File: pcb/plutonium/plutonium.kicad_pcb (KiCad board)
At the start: 2 copper layers, 272.5 x 73.5 mm, 58 parts, among them J1 Conn_01x04, J2 Conn_01x04, K1 diode-choc, K10 diode-choc, K11 diode-choc, K12 diode-choc, K13 diode-choc, K14 diode-choc, K15 diode-choc, K16 diode-choc, K17 diode-choc, K18 diode-choc, K19 diode-choc, K2 diode-choc, K20 diode-choc, K21 diode-choc, K22 diode-choc, K23 diode-choc, K24 diode-choc, K25 diode-choc, K26 diode-choc, K27 diode-choc, K28 diode-choc, K29 diode-choc, K3 diode-choc, K30 diode-choc, K4 diode-choc, K5 diode-choc, K6 diode-choc, K7 diode-choc, K8 diode-choc, K9 diode-choc, U1 xiao-ble, U2 xiao-ble, U3 MT25QL128ABA1ESE

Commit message: [pcb] Plutonium: first revision
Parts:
- removed the REF** at (126.1, 113.2)
- J1, J2: value Conn_01x04 -> debug-port; footprint keeb-libs:debug-port-single-side -> misc:debug-port-single-side
- U1: footprint xiao:xiao-ble-smd -> xiao:xiao-ble-smd-cutout
- moved REF** 73.6 mm to (98.1, 112.7)
- moved REF** 65.6 mm to (203.6, 112.0)
- moved REF** 62.1 mm to (189.6, 112.2)
- moved REF** 48.2 mm to (84.1, 112.7)
- moved BT2 47.9 mm to (171.9, 94.2)
- moved H3 47.9 mm to (155.1, 134.7)
- moved H4 47.9 mm to (155.1, 70.2)
- moved K28 47.9 mm to (172.1, 135.2)
- moved LCD1 47.9 mm to (156.6, 102.7)
- moved R1 47.9 mm to (156.1, 87.2)
- moved REF** 47.9 mm to (173.1, 66.7)
- moved REF** 47.9 mm to (171.9, 66.7)
- moved REF** 47.9 mm to (175.1, 66.7)
- moved U2 47.9 mm to (168.1, 78.5)
- moved U3 47.9 mm to (154.9, 81.7)
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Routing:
- net C1: track 165.7 -> 167.3 mm
- net C1_L: track 173.5 -> 175.1 mm
- net C3_L: track 143.4 -> 144.0 mm
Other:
- board size 272.5 x 73.5 mm -> 278.5 x 73.5 mm

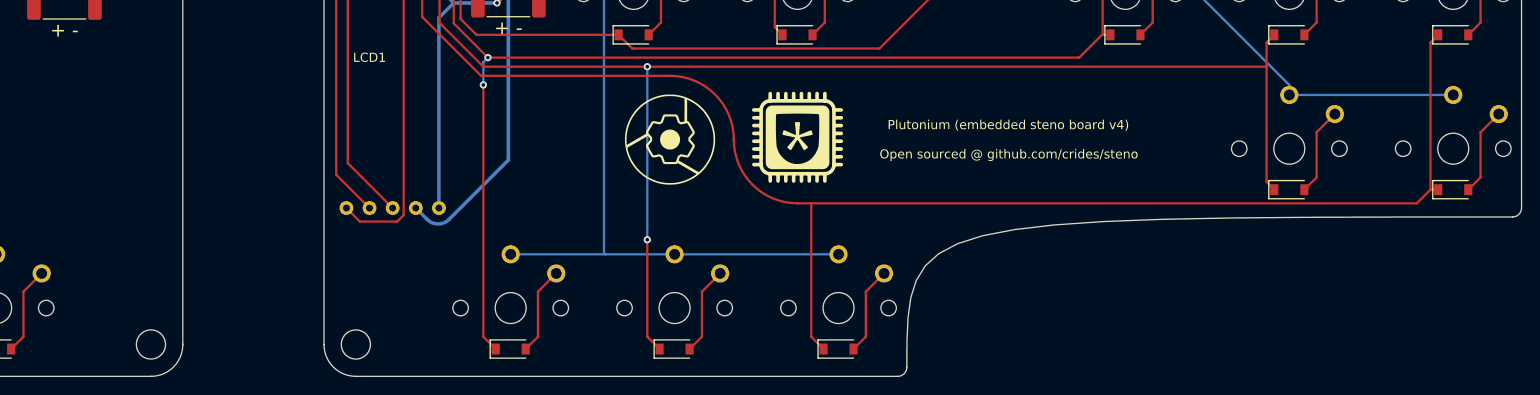
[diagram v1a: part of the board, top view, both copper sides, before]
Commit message: [pcb] Plutonium: add screen mounting and JLC tooling holes
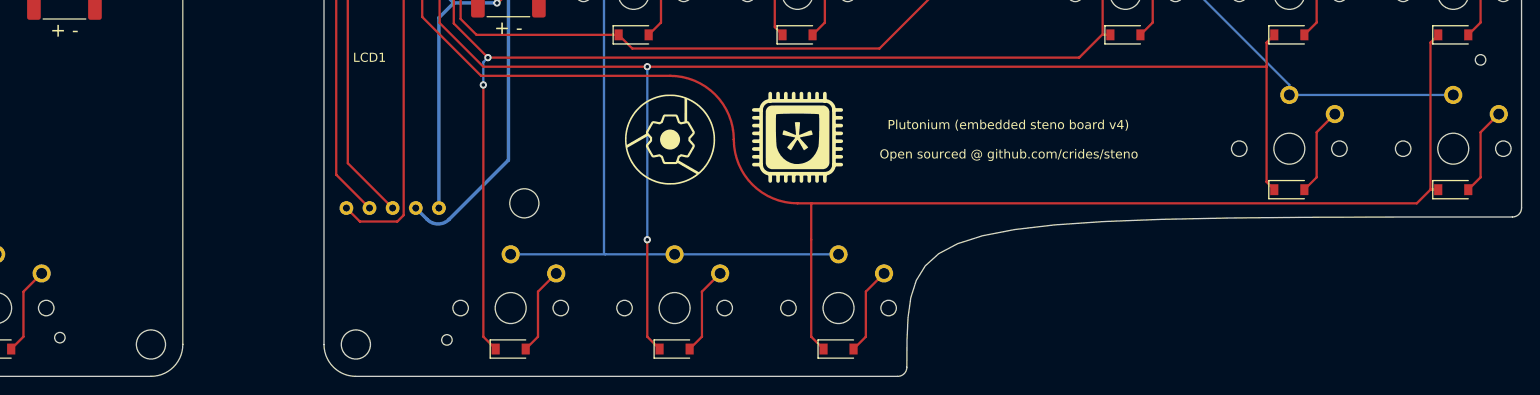
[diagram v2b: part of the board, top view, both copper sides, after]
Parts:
- added REF**: jlc-tooling-hole, misc:jlc-tooling-hole, F.Cu at (122.6, 134.0)
- added REF**: MountingHole_3.2mm_M3, MountingHole:MountingHole_3.2mm_M3, F.Cu at (173.6, 119.2)
- added REF**: jlc-tooling-hole, misc:jlc-tooling-hole, F.Cu at (165.1, 134.2)
- added REF**: jlc-tooling-hole, misc:jlc-tooling-hole, F.Cu at (278.6, 103.5)
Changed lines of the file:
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@@
+  )
+  (footprint "MountingHole:MountingHole_3.2mm_M3" (layer "F.Cu")
+    (at 173.615832 119.20203)
+    (descr "Mounting Hole 3.2mm, no annular, M3")
+    (tags "mounting hole 3.2mm no annular m3")
+    (attr board_only exclude_from_pos_files exclude_from_bom)
+    (fp_text reference "REF**" (at 0 -4.2) (layer "F.SilkS") hide
+      (effects (font (size 1 1) (thickness 0.15)))
+    )
+    (fp_text value "MountingHole_3.2mm_M3" (at 0 4.2) (layer "F.Fab")
+      (effects (font (size 1 1) (thickness 0.15)))
+    )
+    (fp_text user "${REFERENCE}" (at 0.3 0) (layer "F.Fab")
+      (effects (font (size 1 1) (thickness 0.15)))
+    )
+    (fp_circle (center 0 0) (end 3.2 0) (layer "Cmts.User") (width 0.15) (fill none))
+    (fp_circle (center 0 0) (end 3.45 0) (layer "F.CrtYd") (width 0.05) (fill none))
+    (pad "" np_thru_hole circle locked (at 0 0) (size 3.2 3.2) (drill 3.2) (layers *.Cu *.Mask))
   )
   (footprint "MountingHole:MountingHole_3.2mm_M3" (layer "F.Cu")
@@
     (pad "" np_thru_hole circle (at 0 -0.254) (size 0.7874 0.7874) (drill 0.7874) (layers *.Cu *.Mask))
   )
+  (footprint "misc:jlc-tooling-hole" (layer "F.Cu")
+    (at 165.115832 134.20203)
+    (attr through_hole board_only exclude_from_pos_files exclude_from_bom)
+    (fp_text reference "REF**" (at 0 -4 unlocked) (layer "F.SilkS") hide
+      (effects (font (size 1 1) (thickness 0.15)))
+    )
+    (fp_text value "jlc-tooling-hole" (at 0 1.5 unlocked) (layer "F.Fab")
+      (effects (font (size 1 1) (thickness 0.15)))
+    )
+    (pad "" np_thru_hole circle (at 0 0) (size 1.3 1.3) (drill 1.152) (layers *.Mask))
+  )
   (footprint "Connector_JST:JST_PH_S2B-PH-SM4-TB_1x02-1MP_P2.00mm_Horizontal" (layer "F.Cu")
     (at 171.865834 94.202021)
@@
     (pad "4" thru_hole oval (at 3.81 0 90) (size 1.2 1.2) (drill 0.7) (layers *.Cu "F.Mask")
       (net 4 "SWC") (pinfunction "SWC") (pintype "output"))
+  )
+  (footprint "misc:jlc-tooling-hole" (layer "F.Cu")
+    (at 278.615832 103.45203)
+    (attr through_hole board_only exclude_from_pos_files exclude_from_bom)
+    (fp_text reference "REF**" (at 0 -4 unlocked) (layer "F.SilkS") hide
+      (effects (font (size 1 1) (thickness 0.15)))
+    )
+    (fp_text value "jlc-tooling-hole" (at 0 1.5 unlocked) (layer "F.Fab")
+      (effects (font (size 1 1) (thickness 0.15)))
+    )
+    (pad "" np_thru_hole circle (at 0 0) (size 1.3 1.3) (drill 1.152) (layers *.Mask))
   )
   (footprint "Package_SO:SOIC-8_5.23x5.23mm_P1.27mm" (layer "F.Cu")
@@
       (net 14 "+3V3") (pinfunction "3V3") (pintype "power_in"))
   )
+  (footprint "misc:jlc-tooling-hole" (layer "F.Cu")
+    (at 122.615832 133.95203)
+    (attr through_hole board_only exclude_from_pos_files exclude_from_bom)
+    (fp_text reference "REF**" (at 0 -4 unlocked) (layer "F.SilkS") hide
+      (effects (font (size 1 1) (thickness 0.15)))
+    )
+    (fp_text value "jlc-tooling-hole" (at 0 1.5 unlocked) (layer "F.Fab")
+      (effects (font (size 1 1) (thickness 0.15)))
+    )
+    (pad "" np_thru_hole circle (at 0 0) (size 1.3 1.3) (drill 1.152) (layers *.Mask))
+  )
   (footprint "misc:crides-neg" (layer "F.Cu")
